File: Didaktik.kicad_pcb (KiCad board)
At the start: 2 copper layers, 212.7 x 79.4 mm, 104 parts, among them J1 Conn_01x04_MountingPin, SW1 SW_Push, SW10 SW_Push_45deg, SW11 SW_Push_45deg, SW12 SW_Push_45deg, SW13 SW_Push_45deg, SW14 SW_Push_45deg, SW15 SW_Push_45deg, SW16 SW_Push_45deg, SW17 SW_Push_45deg, SW18 SW_Push_45deg, SW19 SW_Push_45deg, SW2 SW_Push_45deg, SW20 SW_Push_45deg, SW21 SW_Push_45deg, SW22 SW_Push_45deg, SW23 SW_Push_45deg, SW24 SW_Push_45deg, SW25 SW_Push_45deg, SW26 SW_Push_45deg, SW27 SW_Push_45deg, SW28 SW_Push_45deg, SW29 SW_Push_45deg, SW3 SW_Push_45deg, SW30 SW_Push_45deg, SW31 SW_Push_45deg, SW32 SW_Push_45deg, SW33 SW_Push_45deg, SW34 SW_Push_45deg, SW35 SW_Push_45deg, SW36 SW_Push_45deg, SW37 SW_Push_45deg, SW38 SW_Push_45deg, SW39 SW_Push_45deg, SW4 SW_Push_45deg, SW40 SW_Push_45deg, SW41 SW_Push_45deg, SW5 SW_Push_45deg, SW6 SW_Push_45deg, SW7 SW_Push_45deg, SW8 SW_Push_45deg, SW9 SW_Push_45deg, U1 ATmega32U4-M, Y1 Crystal_GND24_Small

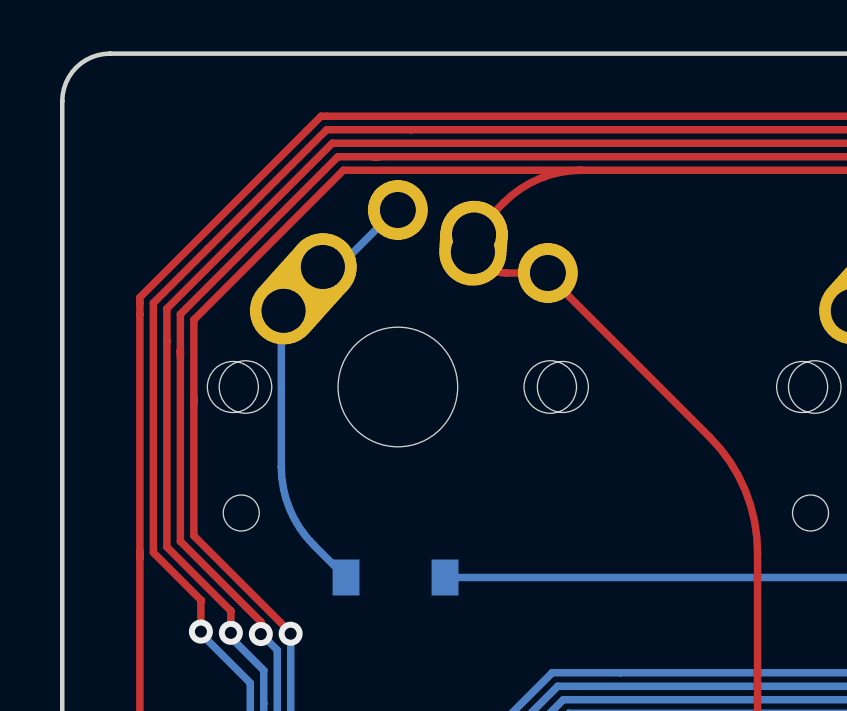
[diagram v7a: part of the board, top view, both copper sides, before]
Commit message: D45 & D40 pcbs created & cleaned. D45 plate created
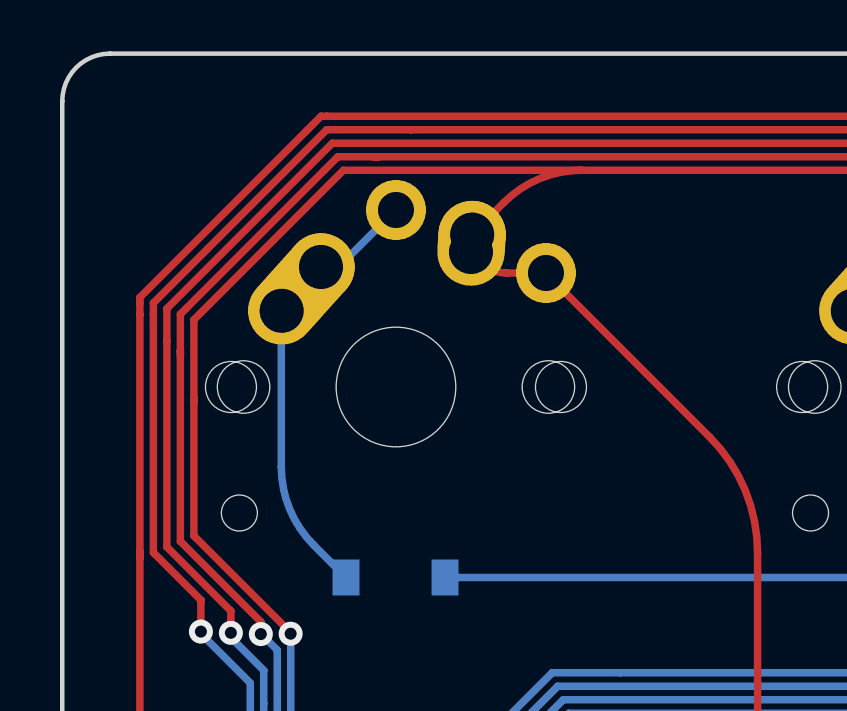
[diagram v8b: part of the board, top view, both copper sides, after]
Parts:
- moved SW2 0.06 mm to (41.3, 41.3)
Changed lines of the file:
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@@
   )
   (footprint "Keebio-Parts:MX-Alps-Choc-1U-NoLED" (layer "F.Cu")
-    (at 41.35 41.275)
+    (at 41.28668 41.275)
     (property "Sheetfile" "Didaktik.kicad_sch")
     (property "Sheetname" "")
